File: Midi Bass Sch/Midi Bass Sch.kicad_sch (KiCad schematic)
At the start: 4 parts

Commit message: updated schematic
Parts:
- removed R?: ValueΩ, symbol Owen's Symbols:Resistor_Mod
- added C?: 10uF, symbol Owen's Symbols:Capacitor
- added D?: LED, symbol Device:LED
- added D?: 4148, symbol Owen's Symbols:Diode
- added R?: 10kΩ, symbol Owen's Symbols:Resistor_Mod
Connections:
- net at U?.1 (RE3/~{MCLR}/Vpp): now also D?.2
- net at J?.5: now also D?.1 (K)
- net at R?.1: now also D?.2 (A)
- new net: C?.1, D?.1, R?.1
- new net +5v: R?.2
- new net GND: C?.2
- no-connect marks 0 -> 1
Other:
- moved on the sheet: J?, R?, U?

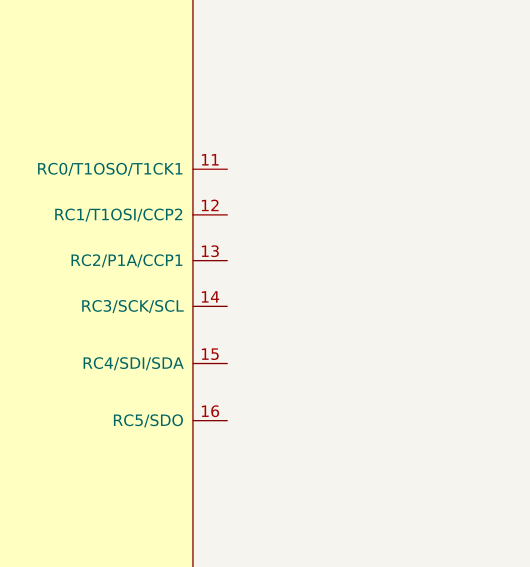
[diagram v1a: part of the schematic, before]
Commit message: updated hours sheet to current
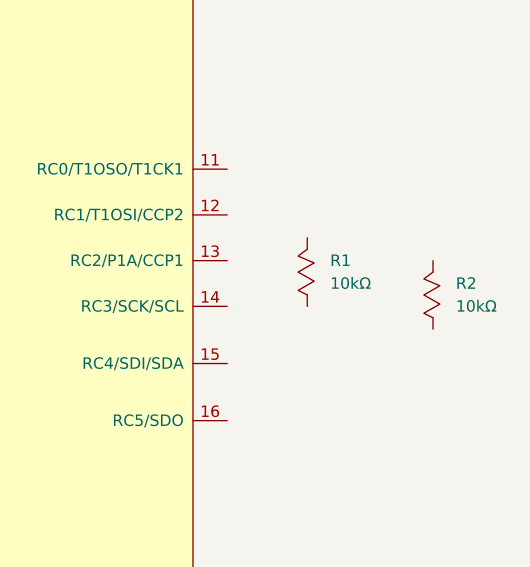
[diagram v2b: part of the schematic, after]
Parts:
- added R1, R2: 10kΩ, symbol Owen's Symbols:Resistor_Mod
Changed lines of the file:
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@@
+	)
+	(symbol
+		(lib_id "Owen's Symbols:Resistor_Mod")
+		(at 148.59 58.42 90)
+		(unit 1)
+		(exclude_from_sim no)
+		(in_bom yes)
+		(on_board yes)
+		(dnp no)
+		(fields_autoplaced yes)
+		(property "Reference" "R1"
+			(at 151.13 57.1499 90)
+			(effects
+				(font
+					(size 1.27 1.27)
+				)
+				(justify right)
+			)
+		)
+		(property "Value" "10kΩ"
+			(at 151.13 59.6899 90)
+			(effects
+				(font
+					(size 1.27 1.27)
+				)
+				(justify right)
+			)
+		)
+		(property "Footprint" ""
+			(at 146.05 59.69 0)
+			(effects
+				(font
+					(size 1.27 1.27)
+				)
+				(hide yes)
+			)
+		)
+		(property "Datasheet" ""
+			(at 146.05 59.69 0)
+			(effects
+				(font
+					(size 1.27 1.27)
+				)
+				(hide yes)
+			)
+		)
+		(property "Description" ""
+			(at 148.59 58.42 0)
+			(effects
+				(font
+					(size 1.27 1.27)
+				)
+				(hide yes)
+			)
+		)
+		(pin "2"
+		)
+		(pin "1"
+		)
+		(instances
+			(project "Midi Bass Sch"
+				(path "/06818073-fb22-48ee-acc5-6dedd827034e"
+					(reference "R1")
+					(unit 1)
+				)
+			)
+		)
 	)
 	(symbol
@@
 					(unit 1)
 				)
+			)
+		)
+	)
+	(symbol
+		(lib_id "Owen's Symbols:Resistor_Mod")
+		(at 162.56 60.96 90)
+		(unit 1)
+		(exclude_from_sim no)
+		(in_bom yes)
+		(on_board yes)
+		(dnp no)
+		(fields_autoplaced yes)
+		(property "Reference" "R2"
+			(at 165.1 59.6899 90)
+			(effects
+				(font
+					(size 1.27 1.27)
+				)
+				(justify right)
+			)
+		)
+		(property "Value" "10kΩ"
+			(at 165.1 62.2299 90)
+			(effects
+				(font
+					(size 1.27 1.27)
+				)
+				(justify right)
+			)
+		)
+		(property "Footprint" ""
+			(at 160.02 62.23 0)
+			(effects
+				(font
+					(size 1.27 1.27)
+				)
+				(hide yes)
+			)
+		)
+		(property "Datasheet" ""
+			(at 160.02 62.23 0)
+			(effects
+				(font
+					(size 1.27 1.27)
+				)
+				(hide yes)
+			)
+		)
+		(property "Description" ""
+			(at 162.56 60.96 0)
+			(effects
+				(font
+					(size 1.27 1.27)
+				)
+				(hide yes)
+			)
+		)
+		(pin "2"
+		)
+		(pin "1"
+		)
+		(instances
+			(project "Midi Bass Sch"
+				(path "/06818073-fb22-48ee-acc5-6dedd827034e"
+					(reference "R2")
+					(unit 1)
+				)
